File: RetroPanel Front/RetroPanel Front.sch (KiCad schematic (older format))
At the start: 16 parts, among them J1 Front Panel, M1 Mounting_Pin, M10 Mounting_Pad, M2 Mounting_Pin, M3 Mounting_Pin, M4 Mounting_Pin, M5 Mounting_Pad, M7 Mounting_Pad, M9 Mounting_Pad, SW1 TURBO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

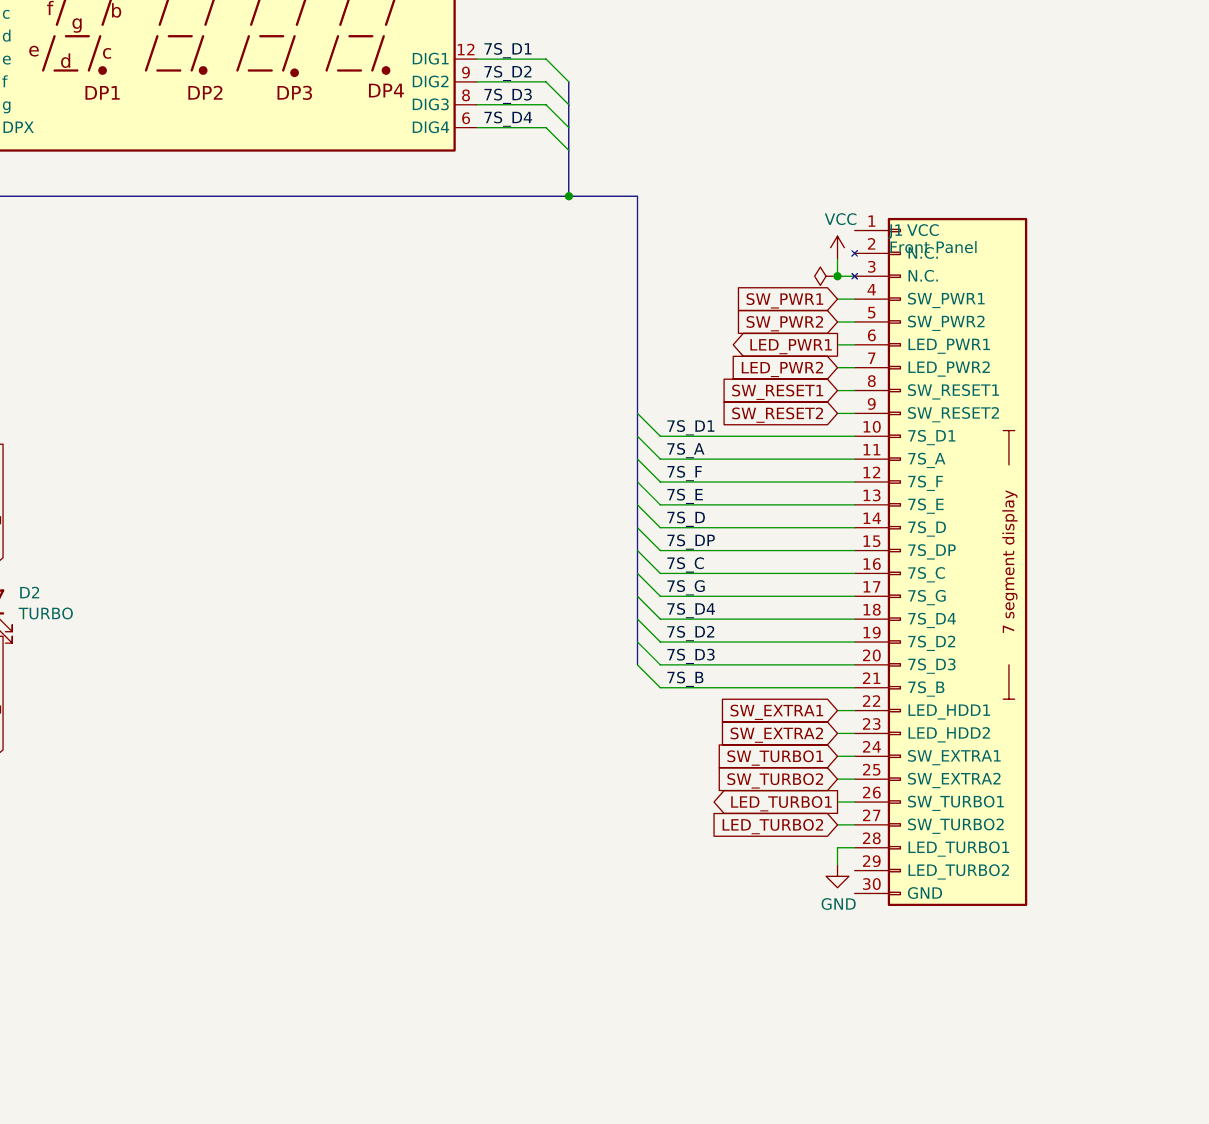
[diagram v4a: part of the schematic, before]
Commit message: Faceplate FP1 and HDD LED
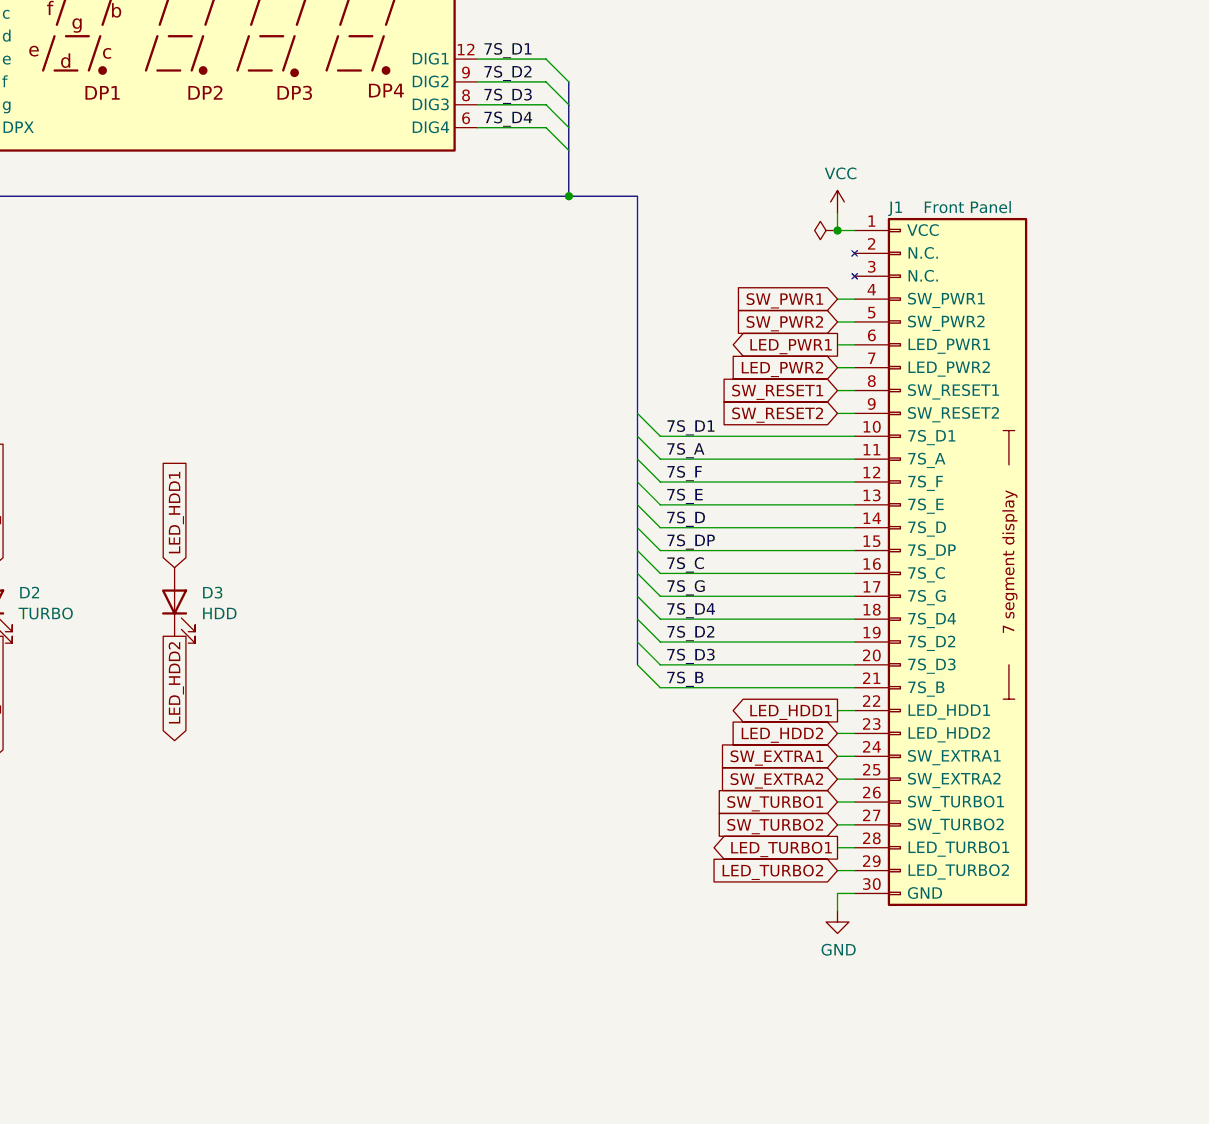
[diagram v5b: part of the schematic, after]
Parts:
- added D3: HDD, LED_THT:LED_D5.0mm, symbol Device:LED
- J1: footprint Connector_PinHeader_2.54mm:PinHeader_1x26_P2.54mm_Horizontal -> Connector_PinHeader_2.54mm:PinHeader_1x30_P2.54mm_Horizontal
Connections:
- net GND: now also J1.30 (GND); no longer J1.28 (LED_TURBO1)
- net LED_TURBO1: now also J1.28 (LED_TURBO1); no longer J1.26 (SW_TURBO1)
- net LED_TURBO2: now also J1.29 (LED_TURBO2); no longer J1.27 (SW_TURBO2)
- net SW_EXTRA1: now also J1.24 (SW_EXTRA1); no longer J1.22 (LED_HDD1)
- net SW_EXTRA2: now also J1.25 (SW_EXTRA2); no longer J1.23 (LED_HDD2)
- net SW_TURBO1: now also J1.26 (SW_TURBO1); no longer J1.24 (SW_EXTRA1)
- net SW_TURBO2: now also J1.27 (SW_TURBO2); no longer J1.25 (SW_EXTRA2)
- net VCC: now also J1.1 (VCC); no longer J1.3 (N.C.)
- new net LED_HDD1: D3.2 (A), J1.22 (LED_HDD1)
- new net LED_HDD2: D3.1 (K), J1.23 (LED_HDD2)
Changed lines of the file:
@@
 U 1 1 62825997
 P 9250 4125
-F 0 "J1" H 9200 5325 50  0000 L CNN
-F 1 "Front Panel" H 9200 5250 50  0000 L CNN
-F 2 "Connector_PinHeader_2.54mm:PinHeader_1x26_P2.54mm_Horizontal" H 9250 4125 50  0001 C CNN
+F 0 "J1" H 9200 5425 50  0000 L CNN
+F 1 "Front Panel" H 9350 5425 50  0000 L CNN
+F 2 "Connector_PinHeader_2.54mm:PinHeader_1x30_P2.54mm_Horizontal" H 9250 4125 50  0001 C CNN
 F 3 "~" H 9250 4125 50  0001 C CNN
 	1    9250 4125
@@
 L power:GND #PWR0101
 U 1 1 6282785A
-P 8975 5700
-F 0 "#PWR0101" H 8975 5450 50  0001 C CNN
-F 1 "GND" H 8980 5527 50  0000 C CNN
-F 2 "" H 8975 5700 50  0001 C CNN
-F 3 "" H 8975 5700 50  0001 C CNN
-	1    8975 5700
+P 8975 5900
+F 0 "#PWR0101" H 8975 5650 50  0001 C CNN
+F 1 "GND" H 8980 5727 50  0000 C CNN
+F 2 "" H 8975 5900 50  0001 C CNN
+F 3 "" H 8975 5900 50  0001 C CNN
+	1    8975 5900
 	1    0    0    -1
 $EndComp
@@
 L power:VCC #PWR0102
 U 1 1 62828DC5
-P 8975 3050
-F 0 "#PWR0102" H 8975 2900 50  0001 C CNN
-F 1 "VCC" H 8990 3223 50  0000 C CNN
-F 2 "" H 8975 3050 50  0001 C CNN
-F 3 "" H 8975 3050 50  0001 C CNN
-	1    8975 3050
+P 8975 2850
+F 0 "#PWR0102" H 8975 2700 50  0001 C CNN
+F 1 "VCC" H 8990 3023 50  0000 C CNN
+F 2 "" H 8975 2850 50  0001 C CNN
+F 3 "" H 8975 2850 50  0001 C CNN
+	1    8975 2850
 	1    0    0    -1
 $EndComp
@@
 	4800 2775 7800 2775
 Wire Wire Line
-	9050 5625 8975 5625
-Wire Wire Line
-	8975 3050 8975 3125
-Wire Wire Line
-	8975 3125 9050 3125
-Wire Wire Line
-	8975 5625 8975 5700
+	9050 5825 8975 5825
+Wire Wire Line
+	8975 2850 8975 2925
+Wire Wire Line
+	8975 2925 9050 2925
+Wire Wire Line
+	8975 5825 8975 5900
 Text GLabel 8975 3225 0    50   Input ~ 0
 SW_PWR1
@@
 Text GLabel 8975 3525 0    50   Input ~ 0
 LED_PWR2
-Text GLabel 8975 5225 0    50   Input ~ 0
+Text GLabel 8975 5425 0    50   Input ~ 0
 SW_TURBO1
-Text GLabel 8975 5325 0    50   Input ~ 0
+Text GLabel 8975 5525 0    50   Input ~ 0
 SW_TURBO2
-Text GLabel 8975 5425 0    50   Output ~ 0
+Text GLabel 8975 5625 0    50   Output ~ 0
 LED_TURBO1
-Text GLabel 8975 5525 0    50   Input ~ 0
+Text GLabel 8975 5725 0    50   Input ~ 0
 LED_TURBO2
 Text GLabel 8975 3625 0    50   Input ~ 0
@@
 L power:PWR_FLAG #FLG0102
 U 1 1 63696E94
-P 8975 3125
-F 0 "#FLG0102" H 8975 3200 50  0001 C CNN
-F 1 "PWR_FLAG" V 8975 3252 50  0001 L CNN
-F 2 "" H 8975 3125 50  0001 C CNN
-F 3 "~" H 8975 3125 50  0001 C CNN
-	1    8975 3125
+P 8975 2925
+F 0 "#FLG0102" H 8975 3000 50  0001 C CNN
+F 1 "PWR_FLAG" V 8975 3052 50  0001 L CNN
+F 2 "" H 8975 2925 50  0001 C CNN
+F 3 "~" H 8975 2925 50  0001 C CNN
+	1    8975 2925
 	0    -1   -1   0
 $EndComp
@@
 Entry Wire Line
 	8200 4125 8100 4025
-Connection ~ 8975 3125
+Connection ~ 8975 2925
 Connection ~ 7800 2775
 Wire Wire Line
@@
 	8975 3725 9050 3725
 Wire Wire Line
-	8975 5225 9050 5225
-Wire Wire Line
-	8975 5325 9050 5325
-Wire Wire Line
 	8975 5425 9050 5425
 Wire Wire Line
 	8975 5525 9050 5525
+Wire Wire Line
+	8975 5625 9050 5625
+Wire Wire Line
+	8975 5725 9050 5725
 Wire Wire Line
 	8200 3825 9050 3825
@@
 Text Notes 3400 7175 0    50   ~ 0
 An extra switch for future proofing (meaning\nI did not know what to do with it).
-Text GLabel 8975 5025 0    50   Input ~ 0
+Text GLabel 8975 5225 0    50   Input ~ 0
 SW_EXTRA1
-Text GLabel 8975 5125 0    50   Input ~ 0
+Text GLabel 8975 5325 0    50   Input ~ 0
 SW_EXTRA2
 Wire Wire Line
-	8975 5025 9050 5025
-Wire Wire Line
-	8975 5125 9050 5125
+	8975 5225 9050 5225
+Wire Wire Line
+	8975 5325 9050 5325
 $Comp
 L mounting:Mounting_Pad M5
@@
 Wire Wire Line
 	10725 1175 10850 1175
+Text GLabel 6075 4700 3    50   Output ~ 0
+LED_HDD2
+Text GLabel 6075 4400 1    50   Input ~ 0
+LED_HDD1
+$Comp
+L Device:LED D3
+U 1 1 635F5BF2
+P 6075 4550
+F 0 "D3" V 6114 4432 50  0000 R CNN
+F 1 "HDD" V 6023 4432 50  0000 R CNN
+F 2 "LED_THT:LED_D5.0mm" H 6075 4550 50  0001 C CNN
+F 3 "~" H 6075 4550 50  0001 C CNN
+	1    6075 4550
+	0    -1   -1   0
+$EndComp
+Text GLabel 8975 5025 0    50   Output ~ 0
+LED_HDD1
+Text GLabel 8975 5125 0    50   Input ~ 0
+LED_HDD2
+Wire Wire Line
+	8975 5125 9050 5125
+Wire Wire Line
+	9050 5025 8975 5025
 Wire Bus Line
 	7800 2275 7800 2775

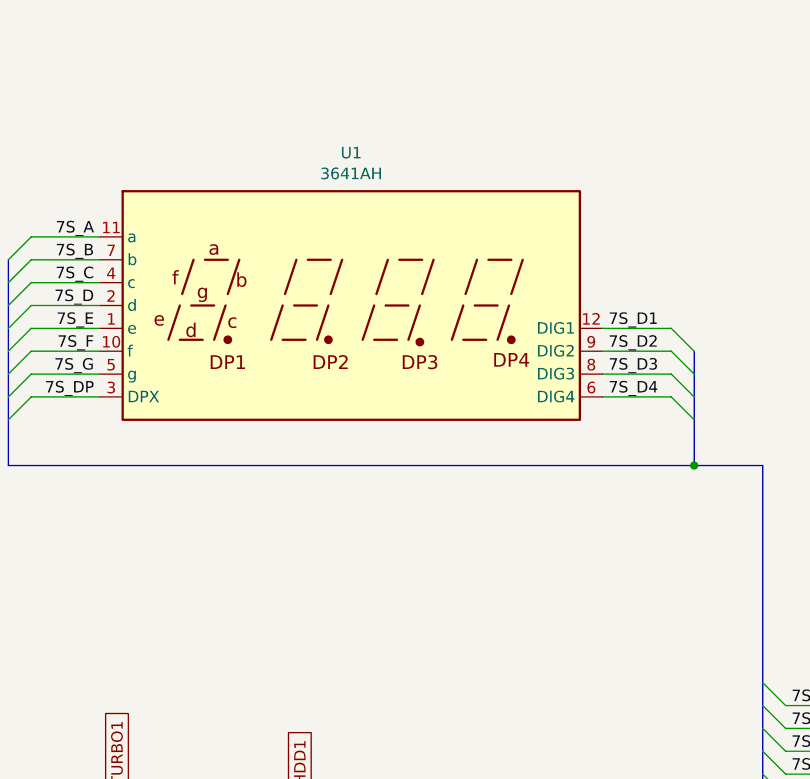
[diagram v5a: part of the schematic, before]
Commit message: Can use both types of displays
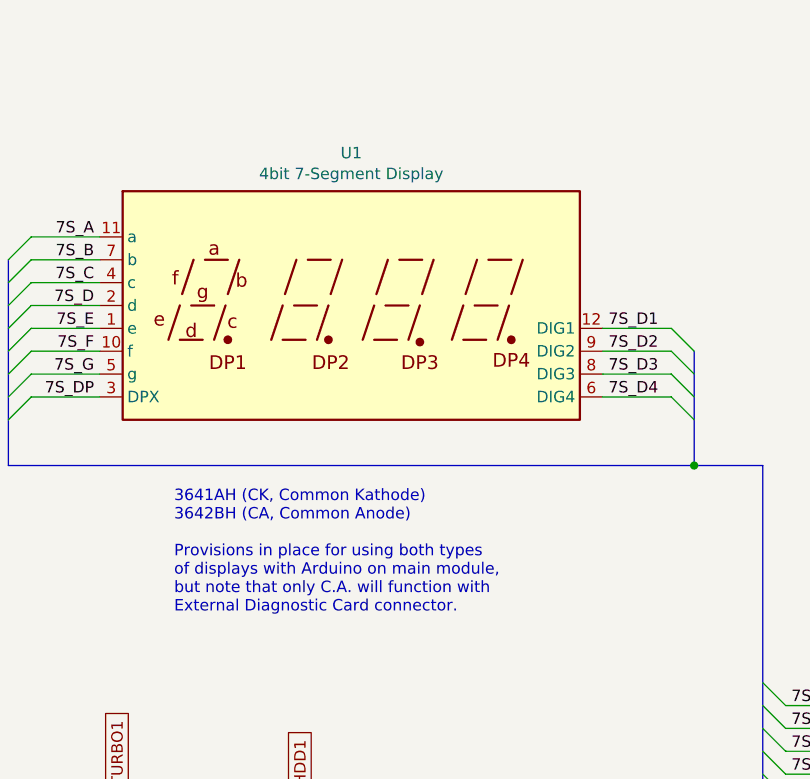
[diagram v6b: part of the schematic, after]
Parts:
- U1: value 3641AH -> 4bit 7-Segment Display
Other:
- note added: "3641AH (CK, Common Kathode)\n3642BH (CA, Common Anode)\n\nProvisions in place for using both types\nof displays with Arduino on main module,\nbut note that only C.A. will function with\nExternal Diagnostic Card connector."
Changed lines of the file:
@@
 P 6300 2075
 F 0 "U1" H 6300 2742 50  0000 C CNN
-F 1 "3641AH" H 6300 2651 50  0000 C CNN
+F 1 "4bit 7-Segment Display" H 6300 2651 50  0000 C CNN
 F 2 "RetroPanel:3641AH" H 6300 1475 50  0001 C CNN
 F 3 "http://www.kingbright.com/attachments/file/psearch/000/00/00/CA56-12CGKWA(Ver.9A).pdf" H 5870 2105 50  0001 C CNN
@@
 Wire Bus Line
 	8100 2775 8100 4825
+Text Notes 5525 3425 0    50   ~ 0
+3641AH (CK, Common Kathode)\n3642BH (CA, Common Anode)\n\nProvisions in place for using both types\nof displays with Arduino on main module,\nbut note that only C.A. will function with\nExternal Diagnostic Card connector.
 $EndSCHEMATC
